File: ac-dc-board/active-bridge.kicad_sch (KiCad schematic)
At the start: 0 parts

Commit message: add parts
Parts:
- added Q1, Q2, Q3, Q4: IPT60R022S7XTMA1, my_Transistor:IPT60R022S7XTMA1, symbol my_Transistor:IPT60R022S7XTMA1
- added U1, U2: 1EDN8550BXTSA1, my_PMIC:1EDN8550BXTSA1, symbol my_PMIC:1EDN8550BXTSA1
- added U3: IR11682STRPBF, my_PMIC:IR11682STRPBF, symbol my_PMIC:IR11682STRPBF

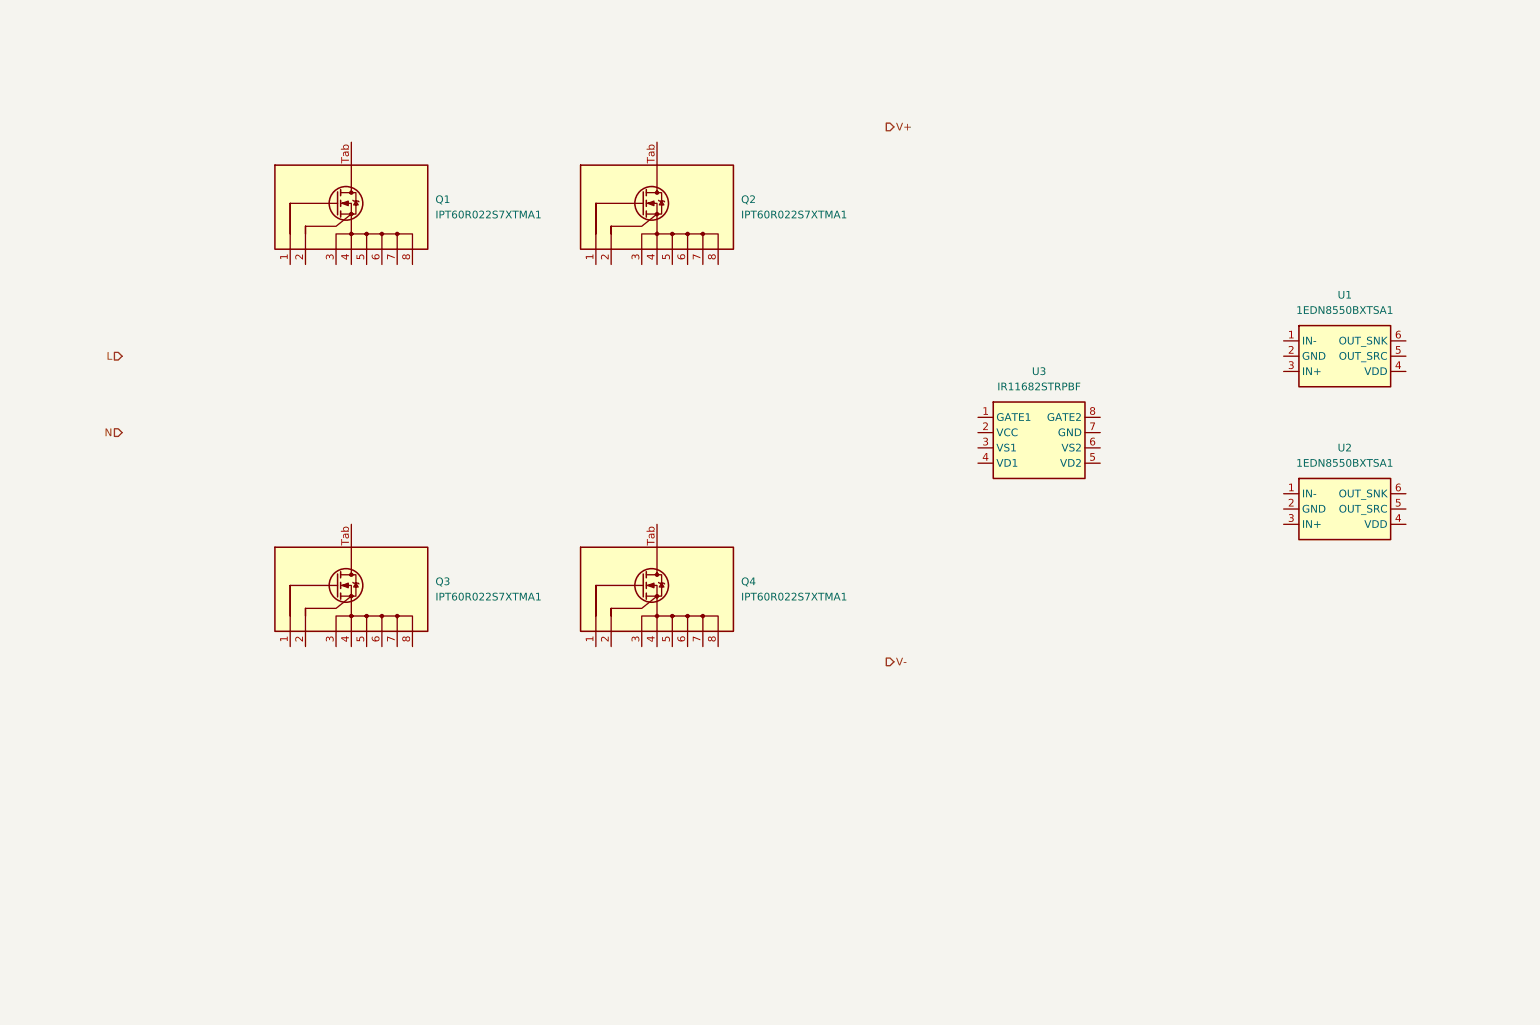
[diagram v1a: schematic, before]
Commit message: designed circuit, not determined constants
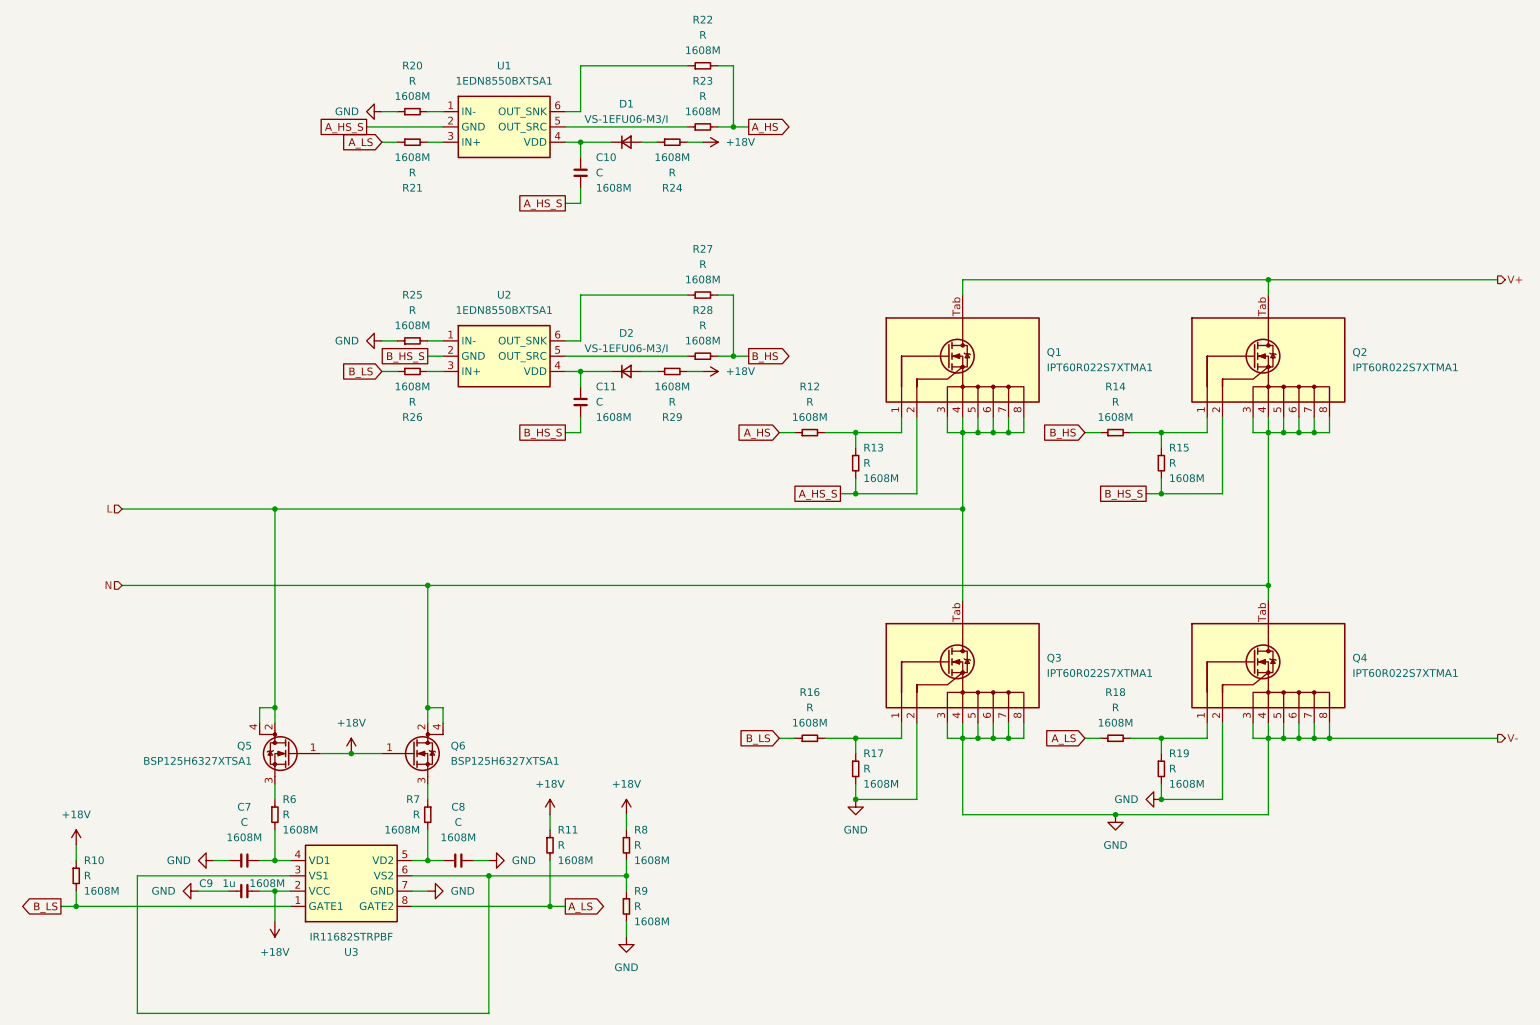
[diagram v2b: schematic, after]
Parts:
- added C10, C11, C7, C8: C, ProjectEV_Capacitor:C_1608M, symbol ProjectEV_Capacitor:C_1608M
- added C9: 1u, ProjectEV_Capacitor:C_1608M, symbol ProjectEV_Capacitor:C_1608M
- added D1, D2: VS-1EFU06-M3/I, my_Diode:VS-1EFU06-M3_I, symbol my_Diode:VS-1EFU06-M3/I
- added Q5, Q6: BSP125H6327XTSA1, my_Transistor:BSP125H6327XTSA1, symbol my_Transistor:BSP125H6327XTSA1
- added R10, R11, R12, R13, R14, R15, R16, R17, R18, R19, R20, R21, R22, R23, R24, R25, R26, R27, R28, R29, R6, R7, R8, R9: R, my_Resistor:R_0603_1608M, symbol my_Resistor:R_0603_1608M
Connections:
- net L: now also Q1.3 (Source), Q1.4 (Source), Q1.5 (Source), Q1.6 (Source), Q1.7 (Source), Q1.8 (Source), Q3.Tab (Drain), Q5.2 (D), Q5.4 (D)
- net N: now also Q2.3 (Source), Q2.4 (Source), Q2.5 (Source), Q2.6 (Source), Q2.7 (Source), Q2.8 (Source), Q4.Tab (Drain), Q6.2 (D), Q6.4 (D)
- net V+: now also Q1.Tab (Drain), Q2.Tab (Drain)
- net at Q2.1 (Gate): now also R14.2, R15.1
- net B_HS_S: now reaches Q2.2 (DriverSource)
- net B_HS_S: now also U2.2 (GND), C11.2, R15.2
- net at Q3.1 (Gate): now also R16.2, R17.1
- net GND: now reaches Q3.2 (DriverSource)
- net GND: now also Q3.3 (Source), Q3.4 (Source), Q3.5 (Source), Q3.6 (Source), Q3.7 (Source), Q3.8 (Source), Q4.2 (DriverSource), Q4.3 (Source), Q4.4 (Source), Q4.5 (Source), Q4.6 (Source), Q4.7 (Source), Q4.8 (Source), U3.7 (GND), C7.1, C8.2, C9.1, R17.2, R19.2, R20.1, R25.1, R9.2
- net B_LS: now reaches U3.1 (GATE1)
- net B_LS: now also R10.2, R16.1, R26.1
- net +18V: now reaches U3.2 (VCC)
- net +18V: now also C9.2, Q5.1 (G), Q6.1 (G), R10.1, R11.1, R24.2, R29.2, R8.1
- net at U3.3 (VS1): now also U3.6 (VS2), R8.2, R9.1
- net at U3.4 (VD1): now also C7.2, R6.2
- net at U3.5 (VD2): now also C8.1, R7.2
- net A_LS: now reaches U3.8 (GATE2)
- net A_LS: now also R11.2, R18.1, R21.1
- net at U2.1 (IN-): now also R25.2
- net at U2.3 (IN+): now also R26.2
- net at U2.4 (VDD): now also C11.1, D2.1 (K)
- net at U2.5 (OUT_SRC): now also R28.1
- net at U2.6 (OUT_SNK): now also R27.1
- net at U1.1 (IN-): now also R20.2
- net A_HS_S: now reaches U1.2 (GND)
- net A_HS_S: now also Q1.2 (DriverSource), C10.2, R13.2
- net at U1.3 (IN+): now also R21.2
- net at U1.4 (VDD): now also C10.1, D1.1 (K)
- net at U1.5 (OUT_SRC): now also R23.1
- net at U1.6 (OUT_SNK): now also R22.1
- net at Q4.1 (Gate): now also R18.2, R19.1
- net at Q1.1 (Gate): now also R12.2, R13.1
- new net: Q6.3 (S), R7.1
- new net: D1.2 (A), R24.1
- new net: Q5.3 (S), R6.1
- new net: D2.2 (A), R29.1
- new net A_HS: R12.1, R22.2, R23.2
- new net B_HS: R14.1, R27.2, R28.2
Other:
- moved on the sheet: Q1, Q2, Q3, Q4, U1, U2, U3
